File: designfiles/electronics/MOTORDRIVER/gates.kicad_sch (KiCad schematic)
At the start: 39 parts, among them IC14 LM5109BSDX_NOPB, IC15 LM5109BSDX_NOPB, IC16 LM5109BSDX_NOPB, IC17 LM5109BSDX_NOPB, IC18 INA2181A2IDGSR, Q22 30V 71A, Q23 30V 71A, Q24 30V 71A, Q25 30V 71A, Q26 30V 71A, Q27 30V 71A, Q28 30V 71A

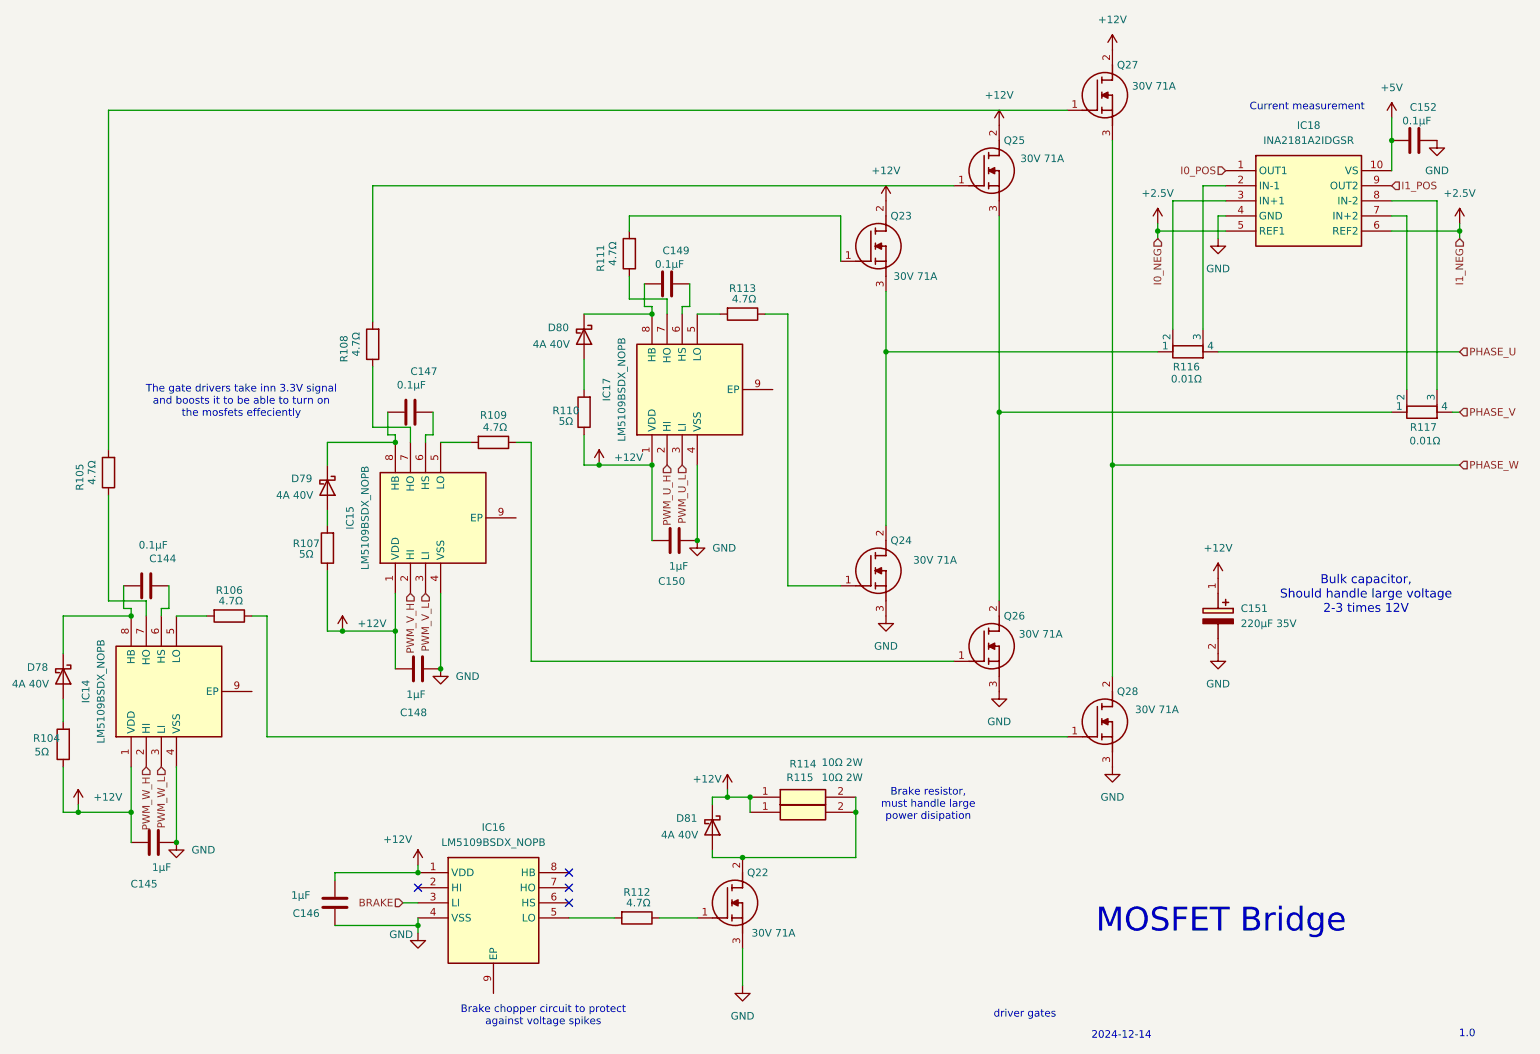
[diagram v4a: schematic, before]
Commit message: added inductors
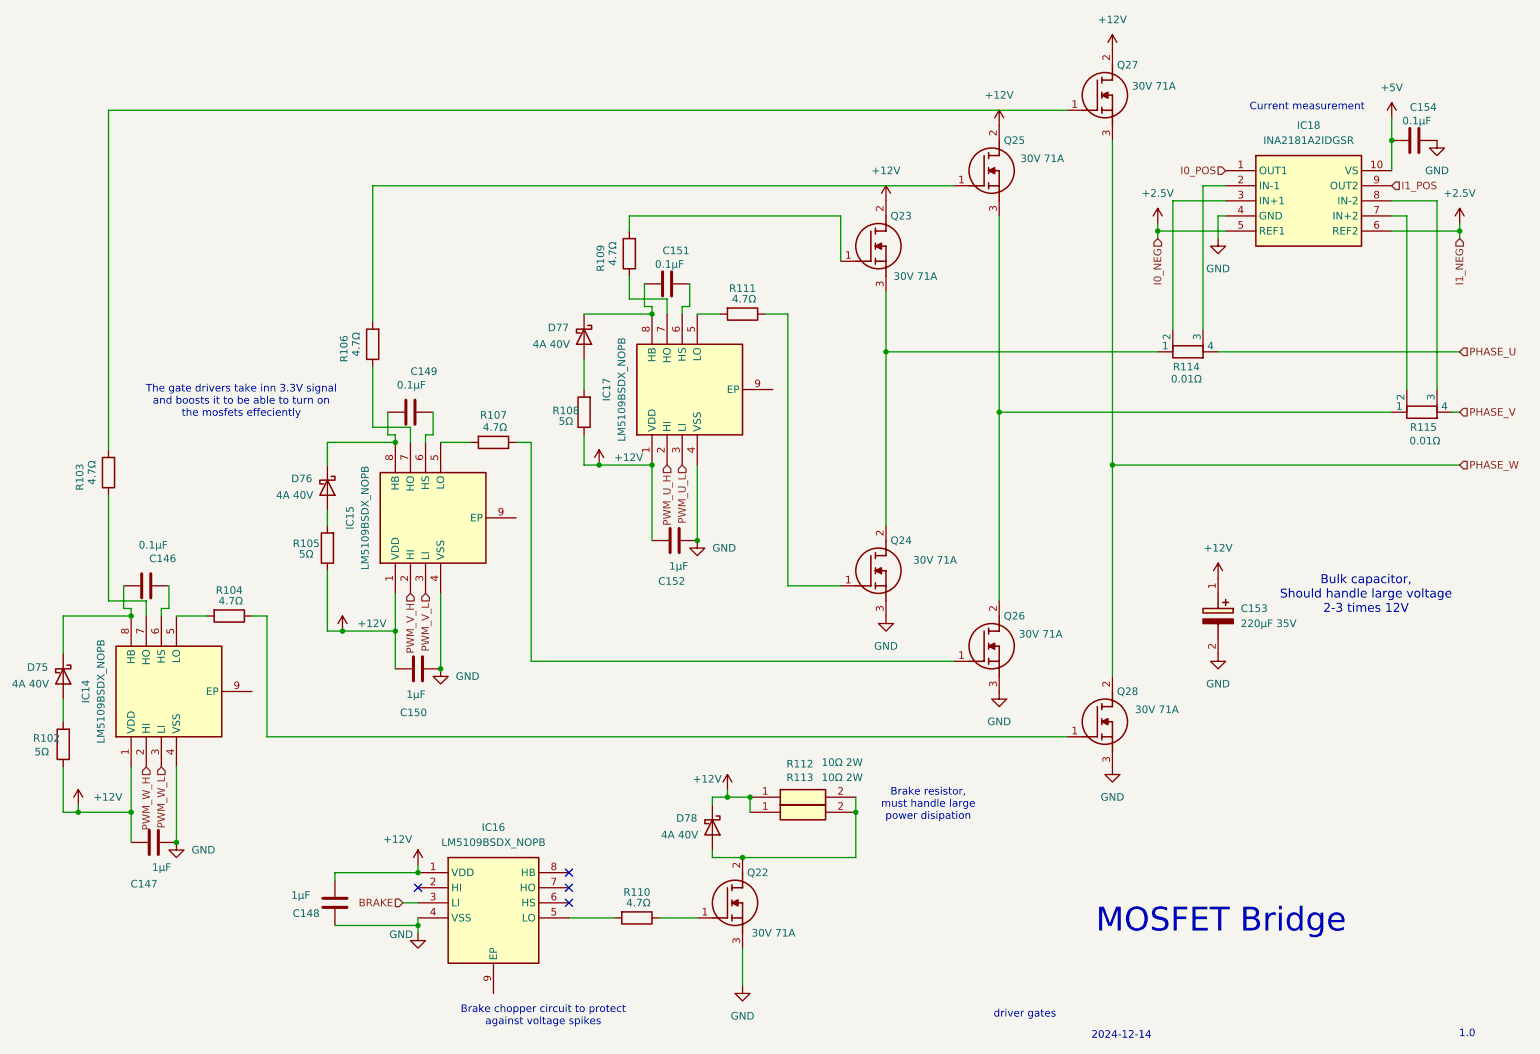
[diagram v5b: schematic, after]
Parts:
- C153: renamed from C151; footprint kuben-footprints:CAPAE1050X1050N -> CAPAE1050X1050N
- IC14, IC15, IC16, IC17: footprint kuben-footprints:SON80P400X400X80-9N -> SON80P400X400X80-9N
- IC18: footprint kuben-footprints:SOP50P490X110-10N -> SOP50P490X110-10N
- Q22, Q23, Q24, Q25, Q26, Q27, Q28: footprint kuben-footprints:IPD047N03LF2SATMA1 -> IPD047N03LF2SATMA1
- R112: renamed from R114; footprint kuben-footprints:RESC3263X80N -> RESC3263X80N
- R113: renamed from R115; footprint kuben-footprints:RESC3263X80N -> RESC3263X80N
- renumbered C144 to C146, C145 to C147, C146 to C148, C147 to C149, C148 to C150, C149 to C151, C150 to C152, C152 to C154, D78 to D75, D79 to D76, D80 to D77, D81 to D78, R104 to R102, R105 to R103, R106 to R104, R107 to R105, R108 to R106, R109 to R107, R110 to R108, R111 to R109, R112 to R110, R113 to R111, R116 to R114, R117 to R115

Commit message: minor tweaks on schematic and started on the pcb layout, made good work
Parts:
- C153: footprint CAPAE1050X1050N -> kuben-footprints:CAPAE1050X1050N
- IC14, IC15, IC16, IC17: footprint SON80P400X400X80-9N -> kuben-footprints:SON80P400X400X80-9N
- IC18: footprint SOP50P490X110-10N -> kuben-footprints:SOP50P490X110-10N
- Q22, Q23, Q24, Q25, Q26, Q27, Q28: footprint IPD047N03LF2SATMA1 -> kuben-footprints:IPD047N03LF2SATMA1
- R112, R113: footprint RESC3263X80N -> kuben-footprints:RESC3263X80N
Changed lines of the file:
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@@
 			)
 		)
-		(property "Footprint" "IPD047N03LF2SATMA1"
+		(property "Footprint" "kuben-footprints:IPD047N03LF2SATMA1"
 			(at 176.53 119.38 0)
 			(effects
@@
 			)
 		)
-		(property "Footprint" "IPD047N03LF2SATMA1"
+		(property "Footprint" "kuben-footprints:IPD047N03LF2SATMA1"
 			(at 195.58 52.07 0)
 			(effects
@@
 			)
 		)
-		(property "Footprint" "SON80P400X400X80-9N"
+		(property "Footprint" "kuben-footprints:SON80P400X400X80-9N"
 			(at 185.09 97.79 0)
 			(effects
@@
 			)
 		)
-		(property "Footprint" "SON80P400X400X80-9N"
+		(property "Footprint" "kuben-footprints:SON80P400X400X80-9N"
 			(at 228.27 76.2 0)
 			(effects
@@
 			)
 		)
-		(property "Footprint" "RESC3263X80N"
+		(property "Footprint" "kuben-footprints:RESC3263X80N"
 			(at 163.83 249.86 0)
 			(effects
@@
 			)
 		)
-		(property "Footprint" "CAPAE1050X1050N"
+		(property "Footprint" "kuben-footprints:CAPAE1050X1050N"
 			(at 132.41 125.73 0)
 			(effects
@@
 			)
 		)
-		(property "Footprint" "IPD047N03LF2SATMA1"
+		(property "Footprint" "kuben-footprints:IPD047N03LF2SATMA1"
 			(at 176.53 64.77 0)
 			(effects
@@
 			)
 		)
-		(property "Footprint" "IPD047N03LF2SATMA1"
+		(property "Footprint" "kuben-footprints:IPD047N03LF2SATMA1"
 			(at 214.63 39.37 0)
 			(effects
@@
 			)
 		)
-		(property "Footprint" "IPD047N03LF2SATMA1"
+		(property "Footprint" "kuben-footprints:IPD047N03LF2SATMA1"
 			(at 195.58 132.08 0)
 			(effects
@@
 			)
 		)
-		(property "Footprint" "IPD047N03LF2SATMA1"
+		(property "Footprint" "kuben-footprints:IPD047N03LF2SATMA1"
 			(at 214.63 144.78 0)
 			(effects
@@
 			)
 		)
-		(property "Footprint" "SON80P400X400X80-9N"
+		(property "Footprint" "kuben-footprints:SON80P400X400X80-9N"
 			(at 140.64 127 0)
 			(effects
@@
 			)
 		)
-		(property "Footprint" "SOP50P490X110-10N"
+		(property "Footprint" "kuben-footprints:SOP50P490X110-10N"
 			(at 254 143.18 0)
 			(effects
@@
 			)
 		)
-		(property "Footprint" "RESC3263X80N"
+		(property "Footprint" "kuben-footprints:RESC3263X80N"
 			(at 163.83 252.4 0)
 			(effects
@@
 			)
 		)
-		(property "Footprint" "SON80P400X400X80-9N"
+		(property "Footprint" "kuben-footprints:SON80P400X400X80-9N"
 			(at 115.57 261.29 0)
 			(effects
@@
 			)
 		)
-		(property "Footprint" "IPD047N03LF2SATMA1"
+		(property "Footprint" "kuben-footprints:IPD047N03LF2SATMA1"
 			(at 152.4 175.26 0)
 			(effects

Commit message: worked on PCB
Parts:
- renumbered C154 to C136, C152 to C137, C151 to C138, C153 to C139, C148 to C141, C150 to C142, C146 to C144, C147 to C145, C149 to C146, D78 to D71, D77 to D72, D75 to D73, D76 to D74, IC17 to IC10, IC16 to IC11, IC14 to IC12, IC15 to IC13, IC18 to IC9, Q23 to Q15, Q25 to Q16, Q27 to Q17, Q22 to Q18, Q24 to Q19, Q26 to Q20, Q28 to Q21, R111 to R100, R104 to R101, R113 to R85, R105 to R86, R108 to R87, R109 to R90, R115 to R91, R106 to R92, R114 to R93, R103 to R95, R112 to R96, R110 to R97, R102 to R98, R107 to R99

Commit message: worked on pcb
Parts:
- removed R91, R93: 0.01Ω, Resistor_SMD:R_0603_1608Metric, symbol Device:R_Shunt
- added R13, R14: 0.01Ω, Resistor_SMD:R_0603_1608Metric, symbol Device:R
- renumbered C144 to C146, C145 to C147, C141 to C148, C146 to C149, C142 to C150, C138 to C151, C137 to C152, C139 to C153, C136 to C154, D73 to D75, D74 to D76, D72 to D77, D71 to D78, IC12 to IC14, IC13 to IC15, IC11 to IC16, IC10 to IC17, IC9 to IC18, Q18 to Q22, Q15 to Q23, Q19 to Q24, Q16 to Q25, Q20 to Q26, Q17 to Q27, Q21 to Q28, R98 to R102, R95 to R103, R101 to R104, R86 to R105, R92 to R106, R99 to R107, R87 to R108, R90 to R109, R97 to R110, R100 to R111, R96 to R112, R85 to R113
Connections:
- net PHASE_U: now also IC18.2 (IN-1), R13.1
- net PHASE_V: now also IC18.8 (IN-2), R14.1
- net at Q23.3 (S), Q24.2 (D): now also IC18.3 (IN+1), R13.2
- net at Q25.3 (S), Q26.2 (D): now also IC18.7 (IN+2), R14.2
